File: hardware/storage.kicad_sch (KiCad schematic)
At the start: 14 parts, among them J6 Micro_SD_Card_Det1, U21 EMMC5.1_BGA153

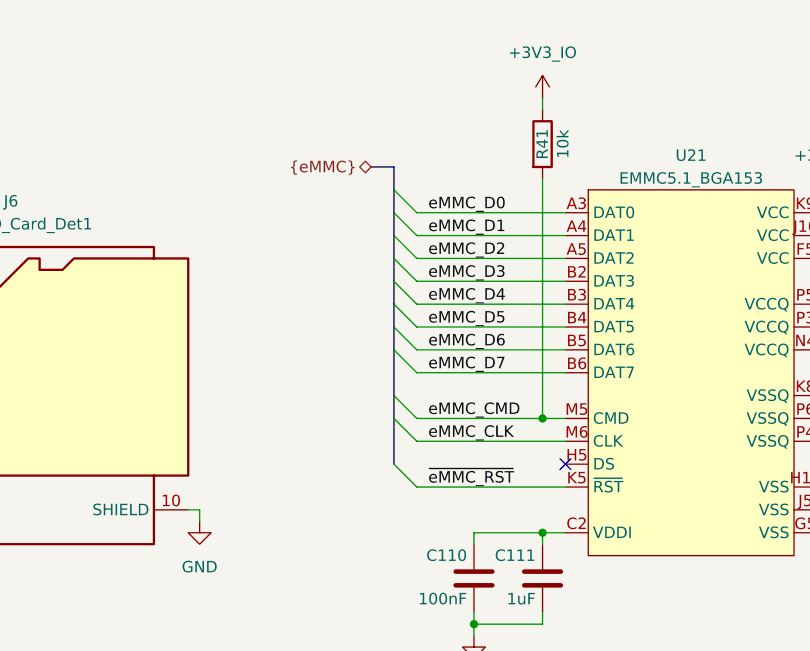
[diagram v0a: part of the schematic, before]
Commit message: Improve heat dissipation and layout
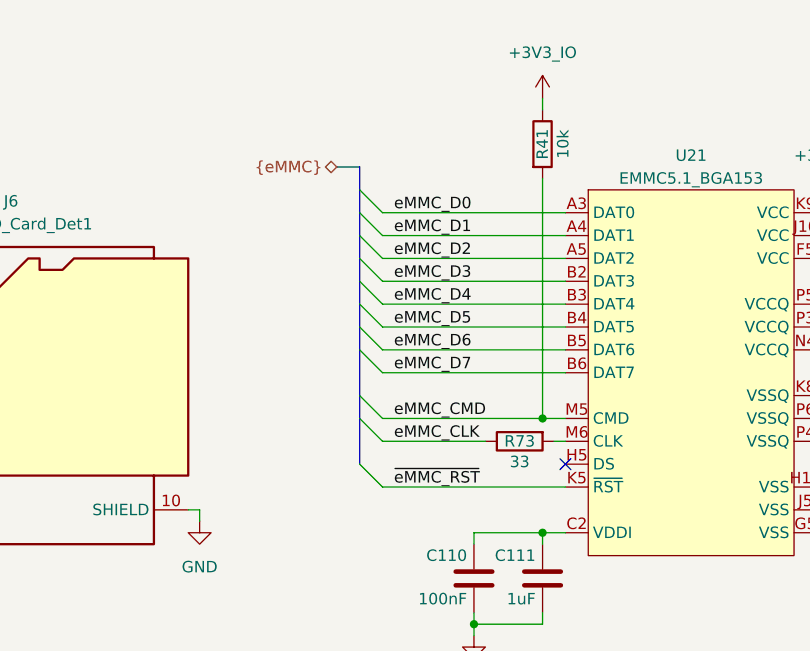
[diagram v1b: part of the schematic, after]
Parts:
- added R73: 33, Resistor_SMD:R_0402_1005Metric, symbol Device:R
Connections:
- net eMMC_CLK: now also R73.1; no longer U21.M6 (CLK)
- new net: R73.2, U21.M6 (CLK)
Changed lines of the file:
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@@
 	)
 	(bus_entry
-		(at 166.37 81.28)
+		(at 162.56 81.28)
 		(size -2.54 -2.54)
 		(stroke
@@
 	)
 	(bus_entry
-		(at 166.37 88.9)
+		(at 162.56 88.9)
 		(size -2.54 -2.54)
 		(stroke
@@
 	)
 	(bus_entry
-		(at 166.37 96.52)
+		(at 162.56 96.52)
 		(size -2.54 -2.54)
 		(stroke
@@
 	)
 	(bus_entry
-		(at 166.37 91.44)
+		(at 162.56 91.44)
 		(size -2.54 -2.54)
 		(stroke
@@
 	)
 	(bus_entry
-		(at 166.37 78.74)
+		(at 162.56 78.74)
 		(size -2.54 -2.54)
 		(stroke
@@
 	)
 	(bus_entry
-		(at 166.37 86.36)
+		(at 162.56 86.36)
 		(size -2.54 -2.54)
 		(stroke
@@
 	)
 	(bus_entry
-		(at 166.37 109.22)
+		(at 162.56 109.22)
 		(size -2.54 -2.54)
 		(stroke
@@
 	)
 	(bus_entry
-		(at 166.37 104.14)
+		(at 162.56 104.14)
 		(size -2.54 -2.54)
 		(stroke
@@
 	)
 	(bus_entry
-		(at 166.37 101.6)
+		(at 162.56 101.6)
 		(size -2.54 -2.54)
 		(stroke
@@
 	)
 	(bus_entry
-		(at 166.37 83.82)
+		(at 162.56 83.82)
 		(size -2.54 -2.54)
 		(stroke
@@
 	)
 	(bus_entry
-		(at 166.37 93.98)
+		(at 162.56 93.98)
 		(size -2.54 -2.54)
 		(stroke
@@
 	(bus
 		(pts
-			(xy 163.83 101.6) (xy 163.83 99.06)
+			(xy 160.02 101.6) (xy 160.02 99.06)
 		)
 		(stroke
@@
 	(wire
 		(pts
-			(xy 166.37 81.28) (xy 182.88 81.28)
+			(xy 162.56 81.28) (xy 182.88 81.28)
 		)
 		(stroke
@@
 	(bus
 		(pts
-			(xy 163.83 86.36) (xy 163.83 83.82)
+			(xy 160.02 86.36) (xy 160.02 83.82)
 		)
 		(stroke
@@
 	(bus
 		(pts
-			(xy 163.83 93.98) (xy 163.83 91.44)
+			(xy 160.02 93.98) (xy 160.02 91.44)
 		)
 		(stroke
@@
 	(bus
 		(pts
-			(xy 163.83 73.66) (xy 161.29 73.66)
+			(xy 160.02 73.66) (xy 157.48 73.66)
 		)
 		(stroke
@@
 	(wire
 		(pts
-			(xy 166.37 88.9) (xy 182.88 88.9)
+			(xy 162.56 88.9) (xy 182.88 88.9)
 		)
 		(stroke
@@
 	(wire
 		(pts
-			(xy 166.37 109.22) (xy 182.88 109.22)
+			(xy 162.56 109.22) (xy 182.88 109.22)
 		)
 		(stroke
@@
 	(bus
 		(pts
-			(xy 163.83 81.28) (xy 163.83 78.74)
+			(xy 160.02 81.28) (xy 160.02 78.74)
 		)
 		(stroke
@@
 	(bus
 		(pts
-			(xy 163.83 78.74) (xy 163.83 76.2)
+			(xy 160.02 78.74) (xy 160.02 76.2)
 		)
 		(stroke
@@
 	(wire
 		(pts
-			(xy 166.37 93.98) (xy 182.88 93.98)
+			(xy 162.56 93.98) (xy 182.88 93.98)
 		)
 		(stroke
@@
 	(wire
 		(pts
-			(xy 166.37 83.82) (xy 182.88 83.82)
+			(xy 162.56 83.82) (xy 182.88 83.82)
 		)
 		(stroke
@@
 	(wire
 		(pts
+			(xy 181.61 104.14) (xy 182.88 104.14)
+		)
+		(stroke
+			(width 0)
+			(type default)
+		)
+	)
+	(wire
+		(pts
 			(xy 212.09 111.76) (xy 212.09 109.22)
 		)
@@
 	(wire
 		(pts
-			(xy 166.37 86.36) (xy 182.88 86.36)
+			(xy 162.56 86.36) (xy 182.88 86.36)
 		)
 		(stroke
@@
 	(wire
 		(pts
-			(xy 166.37 78.74) (xy 182.88 78.74)
+			(xy 162.56 78.74) (xy 182.88 78.74)
 		)
 		(stroke
@@
 	(wire
 		(pts
-			(xy 166.37 91.44) (xy 182.88 91.44)
+			(xy 162.56 91.44) (xy 182.88 91.44)
 		)
 		(stroke
@@
 	(bus
 		(pts
-			(xy 163.83 99.06) (xy 163.83 93.98)
+			(xy 160.02 99.06) (xy 160.02 93.98)
 		)
 		(stroke
@@
 	(bus
 		(pts
-			(xy 163.83 76.2) (xy 163.83 73.66)
+			(xy 160.02 76.2) (xy 160.02 73.66)
 		)
 		(stroke
@@
 	(wire
 		(pts
-			(xy 166.37 96.52) (xy 182.88 96.52)
+			(xy 162.56 96.52) (xy 182.88 96.52)
 		)
 		(stroke
@@
 	(bus
 		(pts
-			(xy 163.83 88.9) (xy 163.83 86.36)
+			(xy 160.02 88.9) (xy 160.02 86.36)
 		)
 		(stroke
@@
 	(bus
 		(pts
-			(xy 163.83 91.44) (xy 163.83 88.9)
+			(xy 160.02 91.44) (xy 160.02 88.9)
 		)
 		(stroke
@@
 	(bus
 		(pts
-			(xy 163.83 101.6) (xy 163.83 106.68)
+			(xy 160.02 101.6) (xy 160.02 106.68)
 		)
 		(stroke
@@
 	(wire
 		(pts
-			(xy 166.37 104.14) (xy 182.88 104.14)
+			(xy 162.56 104.14) (xy 173.99 104.14)
 		)
 		(stroke
@@
 	(bus
 		(pts
-			(xy 163.83 83.82) (xy 163.83 81.28)
+			(xy 160.02 83.82) (xy 160.02 81.28)
 		)
 		(stroke
@@
 	(wire
 		(pts
-			(xy 166.37 101.6) (xy 180.34 101.6)
+			(xy 162.56 101.6) (xy 180.34 101.6)
 		)
 		(stroke
@@
 	)
 	(label "eMMC_D5"
-		(at 167.64 91.44 0)
+		(at 163.83 91.44 0)
 		(effects
 			(font
@@
 	)
 	(label "eMMC_D1"
-		(at 167.64 81.28 0)
+		(at 163.83 81.28 0)
 		(effects
 			(font
@@
 	)
 	(label "eMMC_D3"
-		(at 167.64 86.36 0)
+		(at 163.83 86.36 0)
 		(effects
 			(font
@@
 	)
 	(label "eMMC_CMD"
-		(at 167.64 101.6 0)
+		(at 163.83 101.6 0)
 		(effects
 			(font
@@
 	)
 	(label "eMMC_D4"
-		(at 167.64 88.9 0)
+		(at 163.83 88.9 0)
 		(effects
 			(font
@@
 	)
 	(label "eMMC_CLK"
-		(at 167.64 104.14 0)
+		(at 163.83 104.14 0)
 		(effects
 			(font
@@
 	)
 	(label "eMMC_D0"
-		(at 167.64 78.74 0)
+		(at 163.83 78.74 0)
 		(effects
 			(font
@@
 	)
 	(label "eMMC_D2"
-		(at 167.64 83.82 0)
+		(at 163.83 83.82 0)
 		(effects
 			(font
@@
 	)
 	(label "eMMC_D6"
-		(at 167.64 93.98 0)
+		(at 163.83 93.98 0)
 		(effects
 			(font
@@
 	)
 	(label "eMMC_D7"
-		(at 167.64 96.52 0)
+		(at 163.83 96.52 0)
 		(effects
 			(font
@@
 	)
 	(label "~{eMMC_RST}"
-		(at 167.64 109.22 0)
+		(at 163.83 109.22 0)
 		(effects
 			(font
@@
 	(hierarchical_label "{eMMC}"
 		(shape bidirectional)
-		(at 161.29 73.66 180)
+		(at 157.48 73.66 180)
 		(effects
 			(font
@@
 					(unit 1)
 				)
+			)
+		)
+	)
+	(symbol
+		(lib_id "Device:R")
+		(at 177.8 104.14 90)
+		(mirror x)
+		(unit 1)
+		(exclude_from_sim no)
+		(in_bom yes)
+		(on_board yes)
+		(dnp no)
+		(property "Reference" "R73"
+			(at 177.8 104.14 90)
+			(effects
+				(font
+					(size 1.27 1.27)
+				)
+			)
+		)
+		(property "Value" "33"
+			(at 177.8 106.426 90)
+			(effects
+				(font
+					(size 1.27 1.27)
+				)
+			)
+		)
+		(property "Footprint" "Resistor_SMD:R_0402_1005Metric"
+			(at 177.8 102.362 90)
+			(effects
+				(font
+					(size 1.27 1.27)
+				)
+				(hide yes)
+			)
+		)
+		(property "Datasheet" "~"
+			(at 177.8 104.14 0)
+			(effects
+				(font
+					(size 1.27 1.27)
+				)
+				(hide yes)
+			)
+		)
+		(property "Description" "Resistor"
+			(at 177.8 104.14 0)
+			(effects
+				(font
+					(size 1.27 1.27)
+				)
+				(hide yes)
+			)
+		)
+		(property "LCSC Part #" "C25105"
+			(at 177.8 104.14 90)
+			(effects
+				(font
+					(size 1.27 1.27)
+				)
+				(hide yes)
+			)
+		)
+		(property "FT Position Offset" ""
+			(at 177.8 104.14 90)
+			(effects
+				(font
+					(size 1.27 1.27)
+				)
+				(hide yes)
+			)
+		)
+		(property "FT Rotation Offset" ""
+			(at 177.8 104.14 90)
+			(effects
+				(font
+					(size 1.27 1.27)
+				)
+				(hide yes)
+			)
+		)
+		(pin "1"
+		)
+		(pin "2"
+		)
+		(instances
+			(project "cm0"
+				(path "/b53f5dbb-8078-4818-9e8f-fdf90ba6d854/bbbf0a3c-34ab-4b2d-85d9-faf7e9a88445"
+					(reference "R73")
+					(unit 1)
+				)

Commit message: Add some more decoupling and move trace
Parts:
- J6: FT Position Offset 0,0.381 -> 0,0.081
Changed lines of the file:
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@@
 			)
 		)
-		(property "FT Position Offset" "0,0.381"
+		(property "FT Position Offset" "0,0.081"
 			(at 120.65 99.06 0)
 			(effects
